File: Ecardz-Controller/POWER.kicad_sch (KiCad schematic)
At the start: 23 parts, among them J10 Conn_01x02, J7 Conn_01x02, U2 TPS62160DSG, U3 MIC5504-3.3YM5

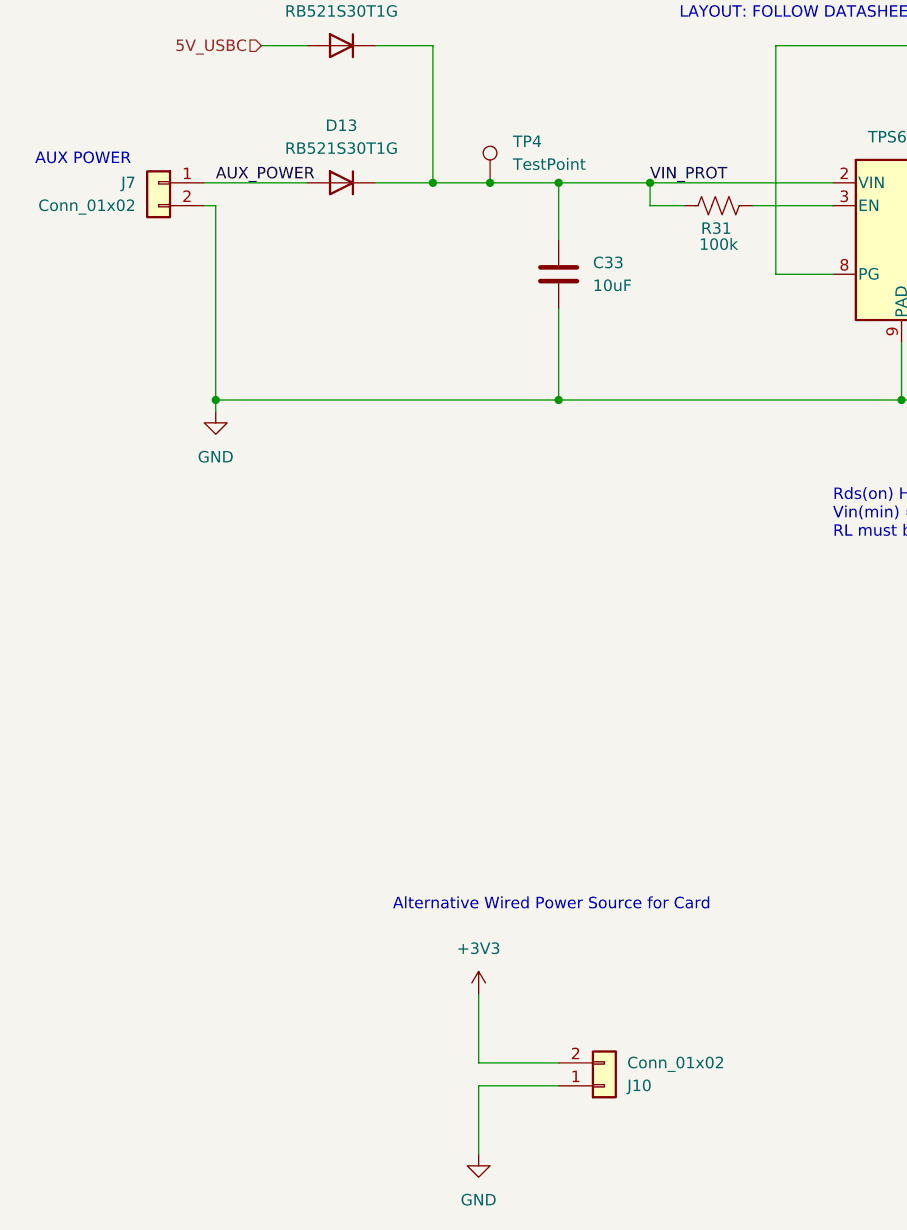
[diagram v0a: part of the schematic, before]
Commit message: moved headers to bottom of board, made J3 DNP
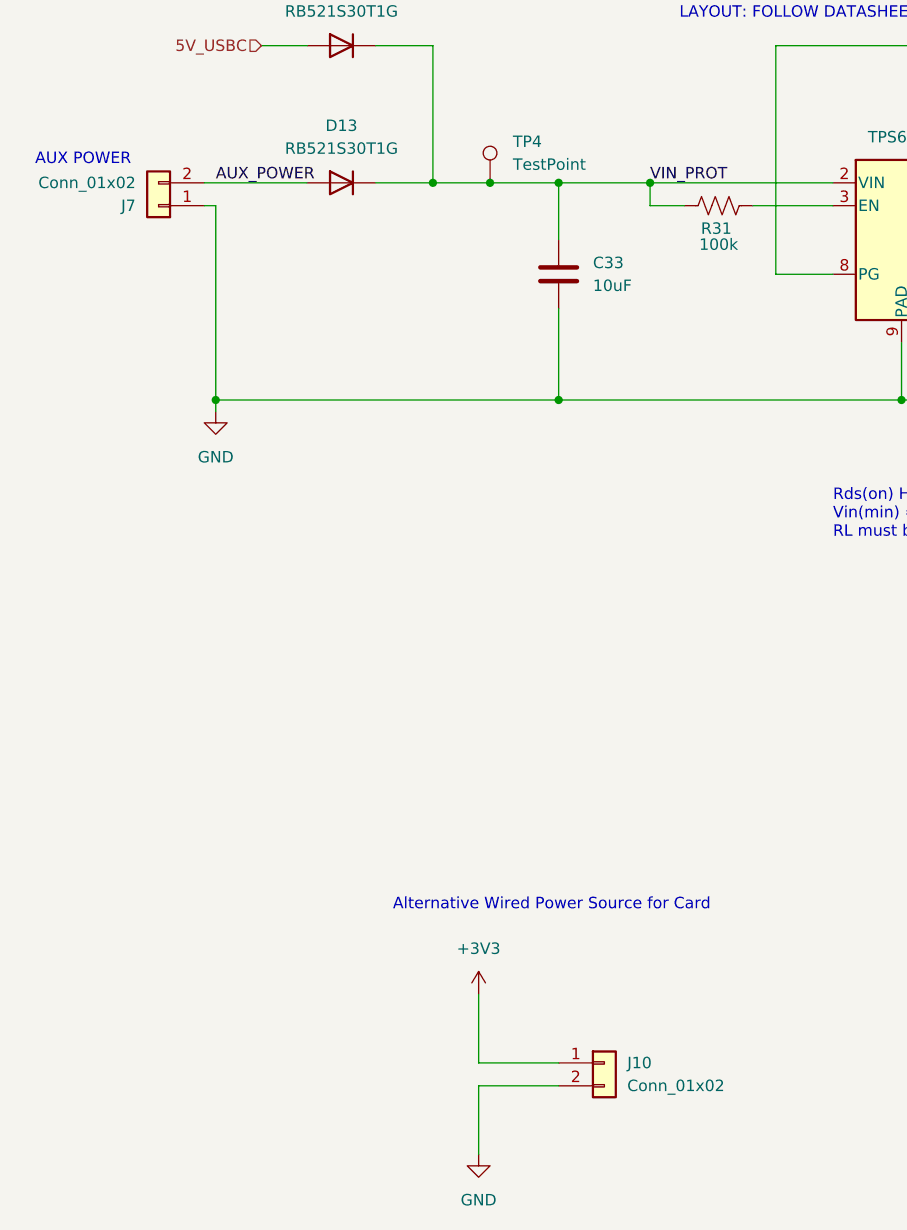
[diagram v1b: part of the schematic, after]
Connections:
- net +3V3: now also J10.1 (Pin_1); no longer J10.2 (Pin_2)
- net AUX_POWER: now also J7.2 (Pin_2); no longer J7.1 (Pin_1)
- net GND: now also J10.2 (Pin_2), J7.1 (Pin_1); no longer J10.1 (Pin_1), J7.2 (Pin_2)
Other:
- moved on the sheet: J7
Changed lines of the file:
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@@
 	(wire
 		(pts
-			(xy 191.77 58.42) (xy 198.12 58.42)
+			(xy 44.45 58.42) (xy 55.88 58.42)
 		)
 		(stroke
@@
 	(wire
 		(pts
-			(xy 180.34 46.99) (xy 179.07 46.99)
+			(xy 191.77 58.42) (xy 198.12 58.42)
 		)
 		(stroke
@@
 	(wire
 		(pts
-			(xy 107.95 68.58) (xy 107.95 43.18)
+			(xy 180.34 46.99) (xy 179.07 46.99)
 		)
 		(stroke
@@
 	(wire
 		(pts
-			(xy 44.45 58.42) (xy 55.88 58.42)
+			(xy 107.95 68.58) (xy 107.95 43.18)
 		)
 		(stroke
@@
 	(wire
 		(pts
+			(xy 74.93 156.21) (xy 83.82 156.21)
+		)
+		(stroke
+			(width 0)
+			(type default)
+		)
+	)
+	(wire
+		(pts
 			(xy 175.26 72.39) (xy 175.26 82.55)
 		)
@@
 	(wire
 		(pts
-			(xy 127 76.2) (xy 127 82.55)
+			(xy 44.45 60.96) (xy 45.72 60.96)
 		)
 		(stroke
@@
 	(wire
 		(pts
-			(xy 152.4 58.42) (xy 158.75 58.42)
+			(xy 127 76.2) (xy 127 82.55)
 		)
 		(stroke
@@
 	(wire
 		(pts
-			(xy 180.34 58.42) (xy 182.88 58.42)
+			(xy 152.4 58.42) (xy 158.75 58.42)
 		)
 		(stroke
@@
 	(wire
 		(pts
-			(xy 83.82 156.21) (xy 74.93 156.21)
+			(xy 180.34 58.42) (xy 182.88 58.42)
 		)
 		(stroke
@@
 	(wire
 		(pts
-			(xy 130.81 43.18) (xy 158.75 43.18)
+			(xy 74.93 158.75) (xy 83.82 158.75)
 		)
 		(stroke
@@
 	(wire
 		(pts
-			(xy 134.62 58.42) (xy 138.43 58.42)
+			(xy 130.81 43.18) (xy 158.75 43.18)
 		)
 		(stroke
@@
 	(wire
 		(pts
-			(xy 121.92 82.55) (xy 124.46 82.55)
+			(xy 134.62 58.42) (xy 138.43 58.42)
 		)
 		(stroke
@@
 	(wire
 		(pts
-			(xy 152.4 82.55) (xy 135.89 82.55)
+			(xy 121.92 82.55) (xy 124.46 82.55)
 		)
 		(stroke
@@
 	(wire
 		(pts
-			(xy 149.86 60.96) (xy 149.86 58.42)
+			(xy 152.4 82.55) (xy 135.89 82.55)
 		)
 		(stroke
@@
 	(wire
 		(pts
-			(xy 83.82 158.75) (xy 74.93 158.75)
+			(xy 149.86 60.96) (xy 149.86 58.42)
 		)
 		(stroke
@@
 	(wire
 		(pts
-			(xy 44.45 60.96) (xy 45.72 60.96)
-		)
-		(stroke
-			(width 0)
-			(type default)
-		)
-	)
-	(wire
-		(pts
 			(xy 74.93 148.59) (xy 74.93 156.21)
 		)
@@
 	(label "VIN_PROT"
 		(at 93.98 58.42 0)
-		(fields_autoplaced yes)
 		(effects
 			(font
@@
 	(label "POWER_GOOD"
 		(at 146.05 43.18 0)
-		(fields_autoplaced yes)
 		(effects
 			(font
@@
 	(label "AUX_POWER"
 		(at 45.72 58.42 0)
-		(fields_autoplaced yes)
 		(effects
 			(font
@@
 		(shape input)
 		(at 50.8 43.18 180)
-		(fields_autoplaced yes)
 		(effects
 			(font
@@
 		(shape input)
 		(at 184.15 34.29 180)
-		(fields_autoplaced yes)
 		(effects
 			(font
@@
 	(symbol
 		(lib_id "Connector_Generic:Conn_01x02")
-		(at 39.37 58.42 0)
-		(mirror y)
+		(at 39.37 60.96 180)
 		(unit 1)
 		(exclude_from_sim no)
@@
 		(dnp no)
 		(property "Reference" "J7"
-			(at 36.83 58.4199 0)
+			(at 36.83 60.9601 0)
 			(effects
 				(font
@@
 		)
 		(property "Value" "Conn_01x02"
-			(at 36.83 60.9599 0)
+			(at 36.83 58.4201 0)
 			(effects
 				(font
@@
 		)
 		(property "Footprint" "Connector_PinHeader_2.54mm:PinHeader_1x02_P2.54mm_Horizontal"
-			(at 39.37 58.42 0)
+			(at 39.37 60.96 0)
 			(effects
 				(font
@@
 		)
 		(property "Datasheet" ""
-			(at 39.37 58.42 0)
+			(at 39.37 60.96 0)
 			(effects
 				(font
@@
 		)
 		(property "Description" "Generic connector, single row, 01x02, script generated (kicad-library-utils/schlib/autogen/connector/)"
-			(at 39.37 58.42 0)
+			(at 39.37 60.96 0)
 			(effects
 				(font
@@
 		)
 		(property "Part Number" "61300211121"
-			(at 39.37 58.42 0)
+			(at 39.37 60.96 0)
 			(effects
 				(font
@@
 	(symbol
 		(lib_id "Connector_Generic:Conn_01x02")
-		(at 88.9 158.75 0)
-		(mirror x)
+		(at 88.9 156.21 0)
 		(unit 1)
 		(exclude_from_sim no)
@@
 		(dnp no)
 		(property "Reference" "J10"
-			(at 91.44 158.7501 0)
+			(at 91.44 156.2099 0)
 			(effects
 				(font
@@
 		)
 		(property "Value" "Conn_01x02"
-			(at 91.44 156.2101 0)
+			(at 91.44 158.7499 0)
 			(effects
 				(font
@@
 		)
 		(property "Footprint" "Connector_PinHeader_2.54mm:PinHeader_1x02_P2.54mm_Horizontal"
-			(at 88.9 158.75 0)
+			(at 88.9 156.21 0)
 			(effects
 				(font
@@
 		)
 		(property "Datasheet" ""
-			(at 88.9 158.75 0)
+			(at 88.9 156.21 0)
 			(effects
 				(font
@@
 		)
 		(property "Description" "Generic connector, single row, 01x02, script generated (kicad-library-utils/schlib/autogen/connector/)"
-			(at 88.9 158.75 0)
+			(at 88.9 156.21 0)
 			(effects
 				(font
@@
 		)
 		(property "Part Number" "61300211121"
-			(at 88.9 158.75 0)
+			(at 88.9 156.21 0)
 			(effects
 				(font
